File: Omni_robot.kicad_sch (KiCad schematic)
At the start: 1 part, among them U1 ESP32-S3-WROOM-1

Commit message: mostly finished schematic
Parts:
- added C10, C11, C9: 22µF, symbol Device:C_Small
- added C12, C13: 0.1µf, symbol Device:C_Small
- added C14, C15: 100nF, symbol Device:C_Small
- added C16, C21, C24: 10µF, symbol Device:C_Polarized
- added C17, C20, C23: 2.2µF, symbol Device:C_Small
- added C18, C19, C22: 0.01µF, symbol Device:C_Small
- added C2: 1 µF, symbol Device:C_Small
- added C3, C4: 4.7 µF, symbol Device:C_Small
- added C5, C6: 10µF, symbol Device:C_Small
- added C7: 0.1µF, symbol Device:C_Small
- added C8: 10pF, symbol Device:C_Small
- added D1, D2: LED_Small, symbol Device:LED_Small
- added D4: PESD5V0S1UL, Diode_SMD:D_SOD-882, symbol Diode:PESD5V0S1UL
- added J1: USB_C_Receptacle_USB2.0_16P, symbol Connector:USB_C_Receptacle_USB2.0_16P
- added J3, J4, J5: M1_Conn_01x06, symbol Connector_Generic:Conn_01x06
- added J6: Battery_Conn_01x03, symbol Connector_Generic:Conn_01x03
- added L1: Coilcraft-XFL4020102MEC, symbol Device:L
- added R1, R2: 22 Ω, symbol Device:R_Small
- added R10, R11: 10 kΩ, symbol Device:R_Small
- added R12: 100 kΩ, symbol Device:R_Small
- added R13, R15, R31: 10kΩ, symbol Device:R_Small
- added R14, R28, R30: 200mΩ, symbol Device:R_Small
- added R16: 100kΩ, symbol Device:R_Small
- added R17: 1 MΩ, symbol Device:R_Small
- added R18: 111kΩ, symbol Device:R_Small
- added R19: 1MΩ, symbol Device:R_Small
- added R20, R21, R22, R23: R_Small, symbol Device:R_Small
- added R24, R25, R26, R27, R29: 0 Ω, symbol Device:R_Small
- added R3, R4: 5.1 kΩ, symbol Device:R_Small
- added R5: 1.13 kΩ, symbol Device:R_Small
- added R6: 1.18 kΩ, symbol Device:R_Small
- added R7: 46.4 kΩ, symbol Device:R_Small
- added R8, R9: 1.5 kΩ, symbol Device:R_Small
- added SW1: SW_SPDT, symbol Switch:SW_SPDT
- added SW2, SW3: SW_SPST, symbol Switch:SW_SPST
- added U2: BQ24074RGT, Package_DFN_QFN:VQFN-16-1EP_3x3mm_P0.5mm_EP1.6x1.6mm, symbol Battery_Management:BQ24074RGT
- added U3: TPS63060, Package_SON:Texas_S-PWSON-N10_ThermalVias, symbol Regulator_Switching:TPS63060
- added U4, U5, U9: DRV8833PWP, Package_SO:HTSSOP-16-1EP_4.4x5mm_P0.65mm_EP3.4x5mm_Mask2.46x2.31mm_ThermalVias, symbol Driver_Motor:DRV8833PWP
- added U7: BMX055, symbol Custom_Sensor_Motion:BMX055
- added U8: TPD2EUSB30, Package_TO_SOT_SMD:Texas_DRT-3, symbol Power_Protection:TPD2EUSB30
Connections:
- net GND: now reaches U1.1 (GND), U1.40 (GND), U1.41 (GND)
- net GND: now also C10.1, C11.1, C12.1, C13.1, C14.1, C15.2, C16.2, C17.1, C2.1, C20.1, C21.2, C23.1, C24.2, C3.2, C4.2, C5.2, C6.2, C7.2, C8.1, C9.1, D4.1 (K), J1.A1 (GND), J1.A12 (GND), J1.B1 (GND), J1.B12 (GND), J1.S1 (SHIELD), J3.2 (Pin_2), J4.2 (Pin_2), J5.2 (Pin_2), J6.3 (Pin_3), R11.2, R12.1, R13.1, R14.1, R15.1, R18.2, R28.1, R3.2, R30.1, R31.1, R4.2, R5.2, R6.1, R7.2, SW1.3 (C), SW2.1 (A), SW3.1 (A), U2.17 (VSS), U2.8 (VSS), U3.11 (PGND), U3.4 (PS/SYNC), U3.7 (GND), U4.13 (GND), U4.17 (GND), U5.13 (GND), U5.17 (GND), U7.12 (SDO2), U7.17 (SDO1), U7.20 (CSB3), U7.4 (GNDA), U7.6 (GNDIO), U8.3 (GND), U9.13 (GND), U9.17 (GND)
- net M2_C1: now reaches U1.10 (IO17)
- net M2_C1: now also J5.3 (Pin_3)
- net M2_C2: now reaches U1.11 (IO18)
- net M2_C2: now also J5.4 (Pin_4)
- net MAG_DRDYM: now reaches U1.12 (IO8)
- net MAG_DRDYM: now also R29.2
- net at U1.13 (USB_D-): now also R2.2
- net at U1.14 (USB_D+): now also R1.1
- net PGOOD: now reaches U1.17 (IO9)
- net PGOOD: now also D2.1 (K), U2.7 (~{PGOOD})
- net CHG: now reaches U1.18 (IO10)
- net CHG: now also D1.1 (K), U2.9 (~{CHG})
- net M1A_IN: now reaches U1.19 (IO11)
- net M1A_IN: now also U4.16 (AIN1), U4.9 (BIN1)
- net +3.3V: now reaches U1.2 (3V3)
- net +3.3V: now also C10.2, C11.2, C14.2, C15.1, C9.2, J3.5 (Pin_5), J4.5 (Pin_5), J5.5 (Pin_5), R17.2, R19.1, R20.2, R21.2, R22.1, R23.1, U3.9 (VOUT), U7.13 (VDDIO), U7.3 (VDD), U7.7 (PS)
- net M1B_IN: now reaches U1.20 (IO12)
- net M1B_IN: now also U4.10 (BIN2), U4.15 (AIN2)
- net M1_C1: now reaches U1.21 (IO13)
- net M1_C1: now also J4.3 (Pin_3)
- net M1_C2: now reaches U1.22 (IO14)
- net M1_C2: now also J4.4 (Pin_4)
- net M2_SLEEP: now reaches U1.23 (IO21)
- net M2_SLEEP: now also R13.2, U9.1 (~{SLEEP})
- net M3_FAULT: now reaches U1.24 (IO47)
- net M3_FAULT: now also U5.8 (~{FAULT})
- net M3_SLEEP: now reaches U1.25 (IO48)
- net M3_SLEEP: now also R15.2, U5.1 (~{SLEEP})
- net ESP_IO0: now reaches U1.27 (IO0)
- net ESP_IO0: now also C13.2, R21.1, SW3.2 (B)
- net M2_FAULT: now reaches U1.28 (IO35)
- net M2_FAULT: now also U9.8 (~{FAULT})
- net ACCEL_INT2: now reaches U1.29 (IO36)
- net ACCEL_INT2: now also R25.2
- net ESP_EN: now reaches U1.3 (EN)
- net ESP_EN: now also C12.2, R20.1, SW2.2 (B)
- net GYRO_INT2: now reaches U1.30 (IO37)
- net GYRO_INT2: now also R27.2
- net M1_SLEEP: now reaches U1.31 (IO38)
- net M1_SLEEP: now also U1.9 (IO16), R31.2, U4.1 (~{SLEEP})
- net M3A_IN: now reaches U1.32 (IO39)
- net M3A_IN: now also U5.16 (AIN1), U5.9 (BIN1)
- net M3B_IN: now reaches U1.33 (IO40)
- net M3B_IN: now also U5.10 (BIN2), U5.15 (AIN2)
- net M3_C1: now reaches U1.34 (IO41)
- net M3_C1: now also J3.3 (Pin_3)
- net M3_C2: now reaches U1.35 (IO42)
- net M3_C2: now also J3.4 (Pin_4)
- net M2B_IN: now reaches U1.38 (IO2)
- net M2B_IN: now also U9.10 (BIN2), U9.15 (AIN2)
- net M2A_IN: now reaches U1.39 (IO1)
- net M2A_IN: now also U9.16 (AIN1), U9.9 (BIN1)
- net SCL: now reaches U1.4 (IO4)
- net SCL: now also R22.2, U7.9 (SCx)
- net SDA: now reaches U1.5 (IO5)
- net SDA: now also R23.2, U7.11 (SDx)
- net ACCEL_INT1: now reaches U1.6 (IO6)
- net ACCEL_INT1: now also R24.2
- net GYRO_INT1: now reaches U1.7 (IO7)
- net GYRO_INT1: now also R26.2
- net M1_FAULT: now reaches U1.8 (IO15)
- net M1_FAULT: now also U4.8 (~{FAULT})
- new net: C19.1, U9.11 (VCP)
- new net: R24.1, U7.19 (INT1)
- new net: R16.2, SW1.2 (B), U3.3 (EN)
- new net: R7.1, U2.14 (TMR)
- new net: C22.1, U5.11 (VCP)
- new net: C23.2, U5.14 (VINT)
- new net: J3.1 (Pin_1), U5.2 (AOUT1), U5.7 (BOUT1)
- new net: R28.2, U5.3 (AISEN), U5.6 (BISEN)
- new net: J3.6 (Pin_6), U5.4 (AOUT2), U5.5 (BOUT2)
- new net: C8.2, R18.1, R19.2, U3.8 (FB)
- new net: J1.B5 (CC2), R4.1
- new net: R14.2, U9.3 (AISEN), U9.6 (BISEN)
- new net: C18.1, U4.11 (VCP)
- new net: C17.2, U4.14 (VINT)
- new net: J4.1 (Pin_1), U4.2 (AOUT1), U4.7 (BOUT1)
- new net: R30.2, U4.3 (AISEN), U4.6 (BISEN)
- new net: J4.6 (Pin_6), U4.4 (AOUT2), U4.5 (BOUT2)
- new net: R6.2, U2.12 (ILIM)
- new net: R11.1, U2.6 (EN1)
- new net: C20.2, U9.14 (VINT)
- new net: R5.1, U2.16 (ISET)
- new net: R12.2, U2.4 (~{CE})
- new net: R10.1, U2.5 (EN2)
- new net: J1.A5 (CC1), R3.1
- new net: R27.1, U7.15 (INT4)
- new net: R29.1, U7.2 (DRDYM)
- new net: R25.1, U7.1 (INT2)
- new net: J5.1 (Pin_1), U9.2 (AOUT1), U9.7 (BOUT1)
- new net: J5.6 (Pin_6), U9.4 (AOUT2), U9.5 (BOUT2)
- new net: R26.1, U7.14 (INT3)
- new net: L1.1, U3.10 (L2)
- new net: L1.2, U3.1 (L1)
- new net: R17.1, U3.5 (PG)
- new net: C7.1, U3.6 (VAUX)
- new net: D1.2 (A), R9.1
- new net: D2.2 (A), R8.2
- new net +BATT: C4.1, J6.1 (Pin_1), U2.2 (BAT), U2.3 (BAT)
- new net D+: J1.A6 (D+), J1.B6 (D+), R1.2, U8.1 (D+)
- new net D-: J1.A7 (D-), J1.B7 (D-), R2.1, U8.2 (D-)
- new net Temp Sense: J6.2 (Pin_2), U2.1 (TS)
- new net USB_5V: C2.2, D4.2 (A), J1.A4 (VBUS), J1.A9 (VBUS), J1.B4 (VBUS), J1.B9 (VBUS), U2.13 (IN)
- new net VSYS: C16.1, C18.2, C19.2, C21.1, C22.2, C24.1, C3.1, C5.1, C6.1, R10.2, R16.1, R8.1, R9.2, U2.10 (OUT), U2.11 (OUT), U3.2 (VIN), U4.12 (VM), U5.12 (VM), U9.12 (VM)
- no-connect marks 0 -> 13
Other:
- note added: "Battery Charger"
- note added: "Buck Booster"
- note added: "ESD Protection"
- note added: "ESP32 S3 WROOM 1"
- note added: "IMU"
- note added: "Motor 1"
- note added: "Motor 2"
- note added: "Motor 3"
- note added: "USB-C Port"
- company: (none) -> Engineering Aesthetic
- title: (none) -> Omni Robot
- moved on the sheet: U1

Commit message: V1 schematic and basic layout
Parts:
- removed C13: 0.1µf, symbol Device:C_Small
- removed J6: Battery_Conn_01x03, symbol Connector_Generic:Conn_01x03
- removed SW2, SW3: SW_SPST, symbol Switch:SW_SPST
- added C1: 0.1µf, Capacitor_SMD:C_0603_1608Metric, symbol Device:C_Small
- added J2: Battery_Conn_01x02, Connector_JST:JST_PH_B2B-PH-K_1x02_P2.00mm_Vertical, symbol Connector_Generic:Conn_01x02
- added R32: 10 kΩ, Resistor_SMD:R_0603_1608Metric, symbol Device:R_Small
- added R33, R34: 0Ω, Resistor_SMD:R_0805_2012Metric, symbol Device:R_Small
- added R35, R36, R37, R38: 0 Ω, Resistor_SMD:R_0805_2012Metric, symbol Device:R_Small
- added SW2, SW4: TSC016A04518A, Custom_Button_Switch_THT:SW-TH_4P-L4.5-W4.5-P3.00-LS4.8, symbol Custom_Button_Switch_THT:TSC016A04518A
- added TP1: Buck out test pad, TestPoint:TestPoint_Pad_D3.0mm, symbol Connector:TestPoint
- added TP2: Buck in test pad, TestPoint:TestPoint_Pad_D3.0mm, symbol Connector:TestPoint
- added TP3: 5v test pad, TestPoint:TestPoint_Pad_D3.0mm, symbol Connector:TestPoint
- C10, C11, C12, C14, C15, C16, C17, C18, C2, C3, C4, C5, C6, C7, C8, C9: footprint (none) -> Capacitor_SMD:C_0603_1608Metric
- C19, C20, C21, C22, C23, C24, D1, D2, R1, R10, R11, R12, R13, R14, R15, R16, R17, R2, R28, R3, R30, R31, R4, R5, R6, R7, R8, R9: footprint (none) -> Resistor_SMD:R_0603_1608Metric
- D4: footprint Diode_SMD:D_SOD-882 -> Resistor_SMD:R_0603_1608Metric
- J1: footprint (none) -> Custom_Connector:USB-C-SMD_TYPE-C16PIN
- J3, J4, J5: footprint (none) -> Connector_JST:JST_GH_BM06B-GHS-TBT_1x06-1MP_P1.25mm_Vertical
- L1: footprint (none) -> Inductor_SMD:L_Coilcraft_XAL4020-XXX
- R18: value 111kΩ -> 200kΩ; footprint (none) -> Resistor_SMD:R_0603_1608Metric
- R19: value 1MΩ -> 1.13MΩ; footprint (none) -> Resistor_SMD:R_0603_1608Metric
- R20, R21: value R_Small -> 10 kΩ; footprint (none) -> Resistor_SMD:R_0603_1608Metric
- R22: value R_Small -> 4.7 kΩ; footprint (none) -> Resistor_SMD:R_0603_1608Metric
- R23: value R_Small -> 4.6 kΩ; footprint (none) -> Resistor_SMD:R_0603_1608Metric
- R24, R25, R26, R27, R29: value 0 Ω -> 0Ω; footprint (none) -> Resistor_SMD:R_0805_2012Metric
- SW1: footprint (none) -> Custom_Button_Switch_THT:SW-TH_SS12D07VG4
- U4, U5, U9: symbol Driver_Motor:DRV8833PWP -> Custom_Driver_Motor:DRV8833PWP
- U7: footprint (none) -> Custom_Sensor_Motion_global:BMX055_EasyEDA
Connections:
- net +3.3V: now also R32.2, TP1.1; no longer R21.2
- net +BATT: now also J2.1 (Pin_1)
- net ESP_EN: now also SW4.4; no longer C12.2
- net ESP_IO0: now also R32.1, SW2.4; no longer R21.1
- net GND: now also R21.2, C1.1, J2.2 (Pin_2), SW2.1, SW2.2, SW4.1, SW4.2
- net Temp Sense: now also R21.1
- net USB_5V: now also TP3.1
- net VSYS: now also TP2.1
- net at J3.1 (Pin_1), U5.2 (AOUT1): now also R38.2; no longer U5.7 (BOUT1)
- net at J3.6 (Pin_6), U5.5 (BOUT2): now also R37.1; no longer U5.4 (AOUT2)
- net at J4.1 (Pin_1), U4.2 (AOUT1): now also R34.2; no longer U4.7 (BOUT1)
- net at J4.6 (Pin_6), U4.5 (BOUT2): now also R33.1; no longer U4.4 (AOUT2)
- net at J5.1 (Pin_1), U9.2 (AOUT1): now also R35.2; no longer U9.7 (BOUT1)
- net at J5.6 (Pin_6), U9.5 (BOUT2): now also R36.1; no longer U9.4 (AOUT2)
- new net: R38.1, U5.7 (BOUT1)
- new net: C12.2, SW4.3
- new net: R37.2, U5.4 (AOUT2)
- new net: R33.2, U4.4 (AOUT2)
- new net: R34.1, U4.7 (BOUT1)
- new net: C1.2, SW2.3
- new net: R36.2, U9.4 (AOUT2)
- new net: R35.1, U9.7 (BOUT1)
- no-connect marks 13 -> 12
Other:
- moved on the sheet: C12, C3, C4, J4, J5, R1, R2, R20, U1

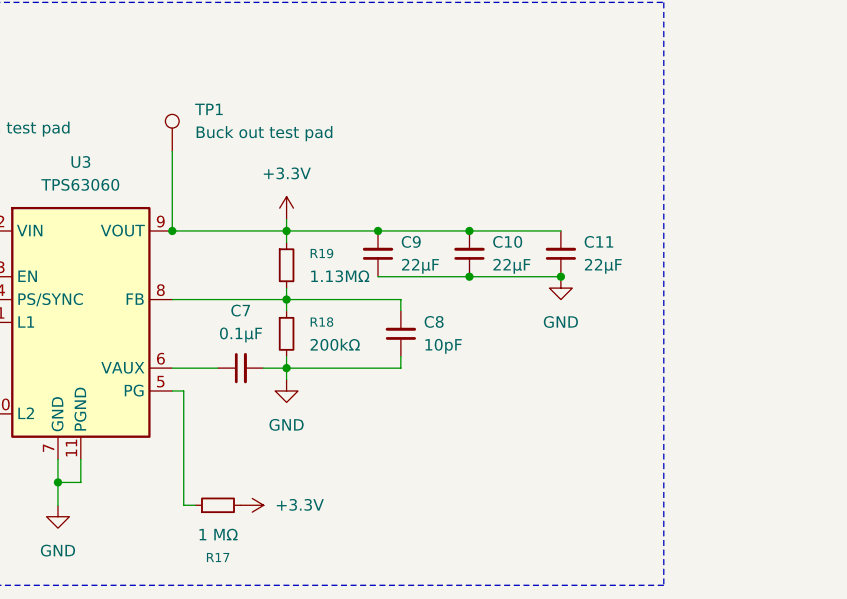
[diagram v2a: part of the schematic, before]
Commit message: Created tracks for motor power
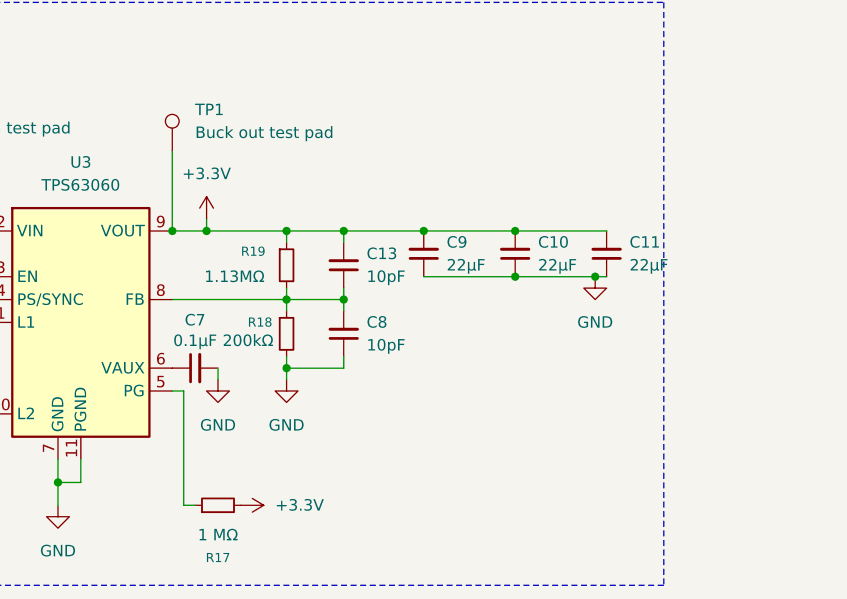
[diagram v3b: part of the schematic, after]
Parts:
- added C13: 10pF, Capacitor_SMD:C_0603_1608Metric, symbol Device:C_Small
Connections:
- net +3.3V: now also C13.2
- net at C8.2, R18.1, R19.2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: now also C13.1
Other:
- moved on the sheet: C10, C11, C7, C8, C9

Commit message: Finished basic tracing
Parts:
- J1: footprint Custom_Connector:USB-C-SMD_TYPE-C16PIN -> Connector_USB:USB_C_Receptacle_Palconn_UTC16-G
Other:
- moved on the sheet: C10, C11, C13, C5, C6, C7, C8, C9, L1, R16, R17, R18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
